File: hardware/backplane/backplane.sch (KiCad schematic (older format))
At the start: 106 parts, among them J1 C96ABC, J10 Conn_Coaxial_Power, J2 C96ABC, J3 C96ABC, J4 C96ABC, J5 C96ABC, J6 C96ABC, J7 C96ABC, J8 C96ABC, J9 C96ABC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

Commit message: update schematics for backplane and base to put PHI_2 on the bus
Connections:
- net PHI_2 is gone; now on net A28: U8.8
- net A28: no longer U1.3, U4.6, U8.5
- net C31 renamed BASE_CLK
- net BASE_CLK: now also U1.3, U4.6, U8.5; no longer D3.1 (K), D5.1 (K), R1.2, SW4.2
- new net ~RST_HDR~: D3.1 (K), D5.1 (K), R1.2, SW4.2
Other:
- note added: "Clock switcher"
- note added: "TODO: put PHI_2 on the bus - bus devices could use this to ensure\nthat they have a consistent view on what the effective clock speed \nof the system\nMaybe put it at A28 and move BASE_CLK to C31 to replace ~RST_HDR~\n~RST_HDR~ is unnecessary as the reset signal is handled by a header on the backplane"
- note removed: "TODO: put PHI_2 on the bus - bus devices could use this to ensure\nthat they have a consistent view on what the effective clock speed \nof the system is\nMaybe put it at A28 and move BASE_CLK to C31 to replace ~RST_HDR~\n~RST_HDR~ is unnecessary as the reset signal is handled by a header on the backplane"
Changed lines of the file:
@@
 	1    0    0    -1
 $EndComp
-Text Notes 3200 1600 0    50   ~ 0
-shorter clock rst pulse s.t. \nclock starts before other ICs
 Text GLabel 3150 1200 2    50   Input ~ 0
 ~RST~
@@
 Wire Wire Line
 	10800 1650 10700 1650
-Text GLabel 10700 1500 0    50   Input ~ 0
-BASE_CLK
 Text GLabel 10800 1500 2    50   Input ~ 0
 A28
@@
 NoConn ~ 14450 2750
 Text Notes 9600 550  0    50   ~ 0
-TODO: put PHI_2 on the bus - bus devices could use this to ensure\nthat they have a consistent view on what the effective clock speed \nof the system is\nMaybe put it at A28 and move BASE_CLK to C31 to replace ~RST_HDR~\n~RST_HDR~ is unnecessary as the reset signal is handled by a header on the backplane
+TODO: put PHI_2 on the bus - bus devices could use this to ensure\nthat they have a consistent view on what the effective clock speed \nof the system\nMaybe put it at A28 and move BASE_CLK to C31 to replace ~RST_HDR~\n~RST_HDR~ is unnecessary as the reset signal is handled by a header on the backplane
 $Comp
 L Device:C CBX1
@@
 F 3 "" H 16050 1800 50  0001 C CNN
 	1    16050 1800
-	0    1    1    0
+	0    1    -1   0
 $EndComp
 $Comp
@@
 TODO: overvoltage protection\n(not doing this for now)
 Connection ~ 10100 4400
-Text GLabel 10650 2400 0    50   Input ~ 0
-~RST_HDR~
 Text GLabel 10850 2400 2    50   Input ~ 0
 C31
@@
 Text Notes 9600 100  0    50   ~ 0
 BASE_CLK is the clock signal generated by the crystal oscillator or the 555\nPHI_2 is the effective clock signal, which may be controlled by a bus device if ~BUS_ACTIVE~ is low
+Text GLabel 10650 2400 0    50   Input ~ 0
+BASE_CLK
+Text GLabel 10700 1500 0    50   Input ~ 0
+PHI_2
+Text Notes 6450 600  0    50   ~ 10
+Clock switcher
+Text Notes 3250 1600 0    50   ~ 0
+shorter clock rst pulse s.t. \nclock starts before other ICs
 $EndSCHEMATC

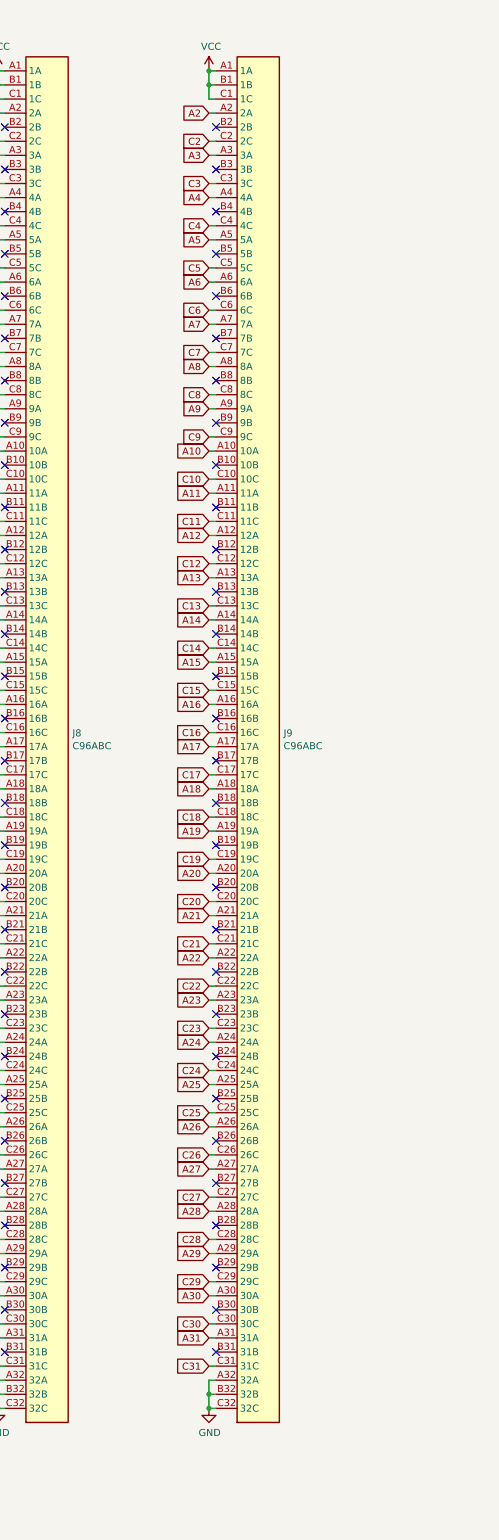
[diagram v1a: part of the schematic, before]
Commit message: shift fp connector to other side of backplane
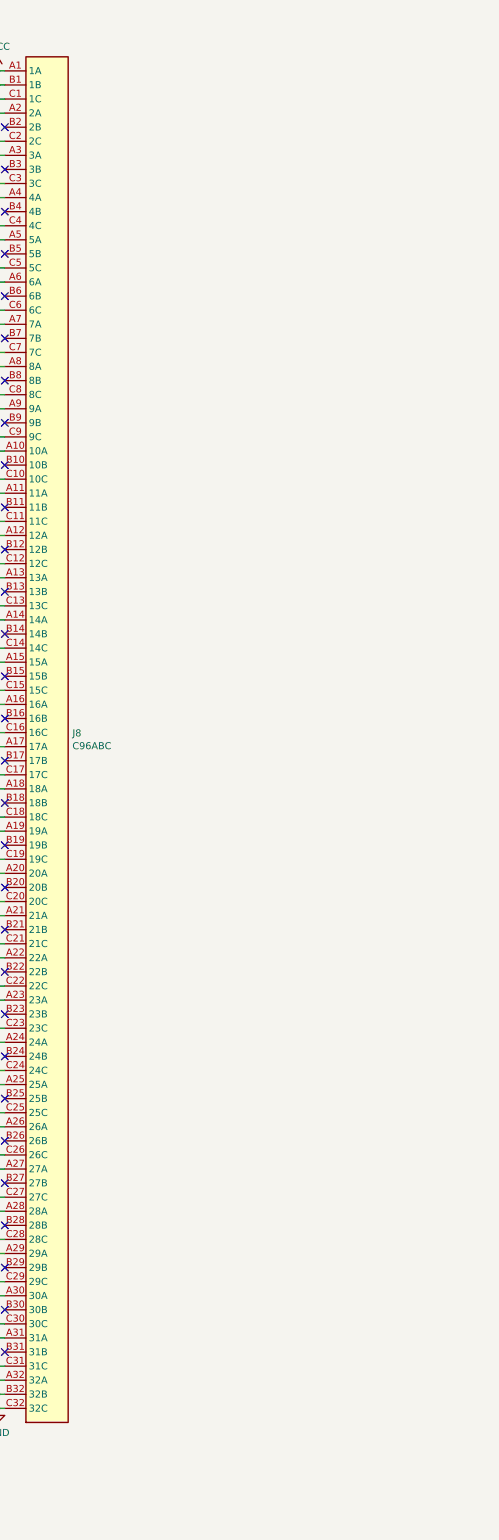
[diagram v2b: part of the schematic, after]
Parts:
- removed J9: C96ABC, Connector_DIN:DIN41612_C_3x32_Female_Vertical_THT, symbol Connector:C96ABC
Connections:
- no-connect marks 69 -> 39

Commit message: backplane relayout 1
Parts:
- J10: footprint Connector_Phoenix_MSTB:PhoenixContact_MSTBVA_2,5_2-G-5,08_1x02_P5.08mm_Vertical -> Connector_AMASS:AMASS_XT60-M_1x02_P7.20mm_Vertical
- Q1, Q2, Q3: footprint Package_TO_SOT_THT:TO-220-3_Horizontal_TabDown -> Package_TO_SOT_THT:TO-220-3_Vertical

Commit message: FP WIP
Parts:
- added H5, H6: MountingHole, rails:m5-close, symbol Mechanical:MountingHole
- added J? (x2): Conn_02x01, symbol Connector_Generic:Conn_02x01
- added R? (x2): 1k, Resistor_THT:R_Axial_DIN0207_L6.3mm_D2.5mm_P7.62mm_Horizontal, symbol Device:R
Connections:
- net +5V: now also J?.1 (Pin_1)
- net GND: now also R?.1, R?.1
- net VCC: now also J?.1 (Pin_1)
- new net: J?.2 (Pin_2), R?.2 (x2)
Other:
- moved on the sheet: D2, D4, H1, H2, H3, H4, R15, R16
